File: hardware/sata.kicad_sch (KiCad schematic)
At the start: 26 parts, among them IC1 ASM1061, J9 SATA_22pin, Q2 FDS4435BZ, Q3 FDS4435BZ, Y1 Crystal

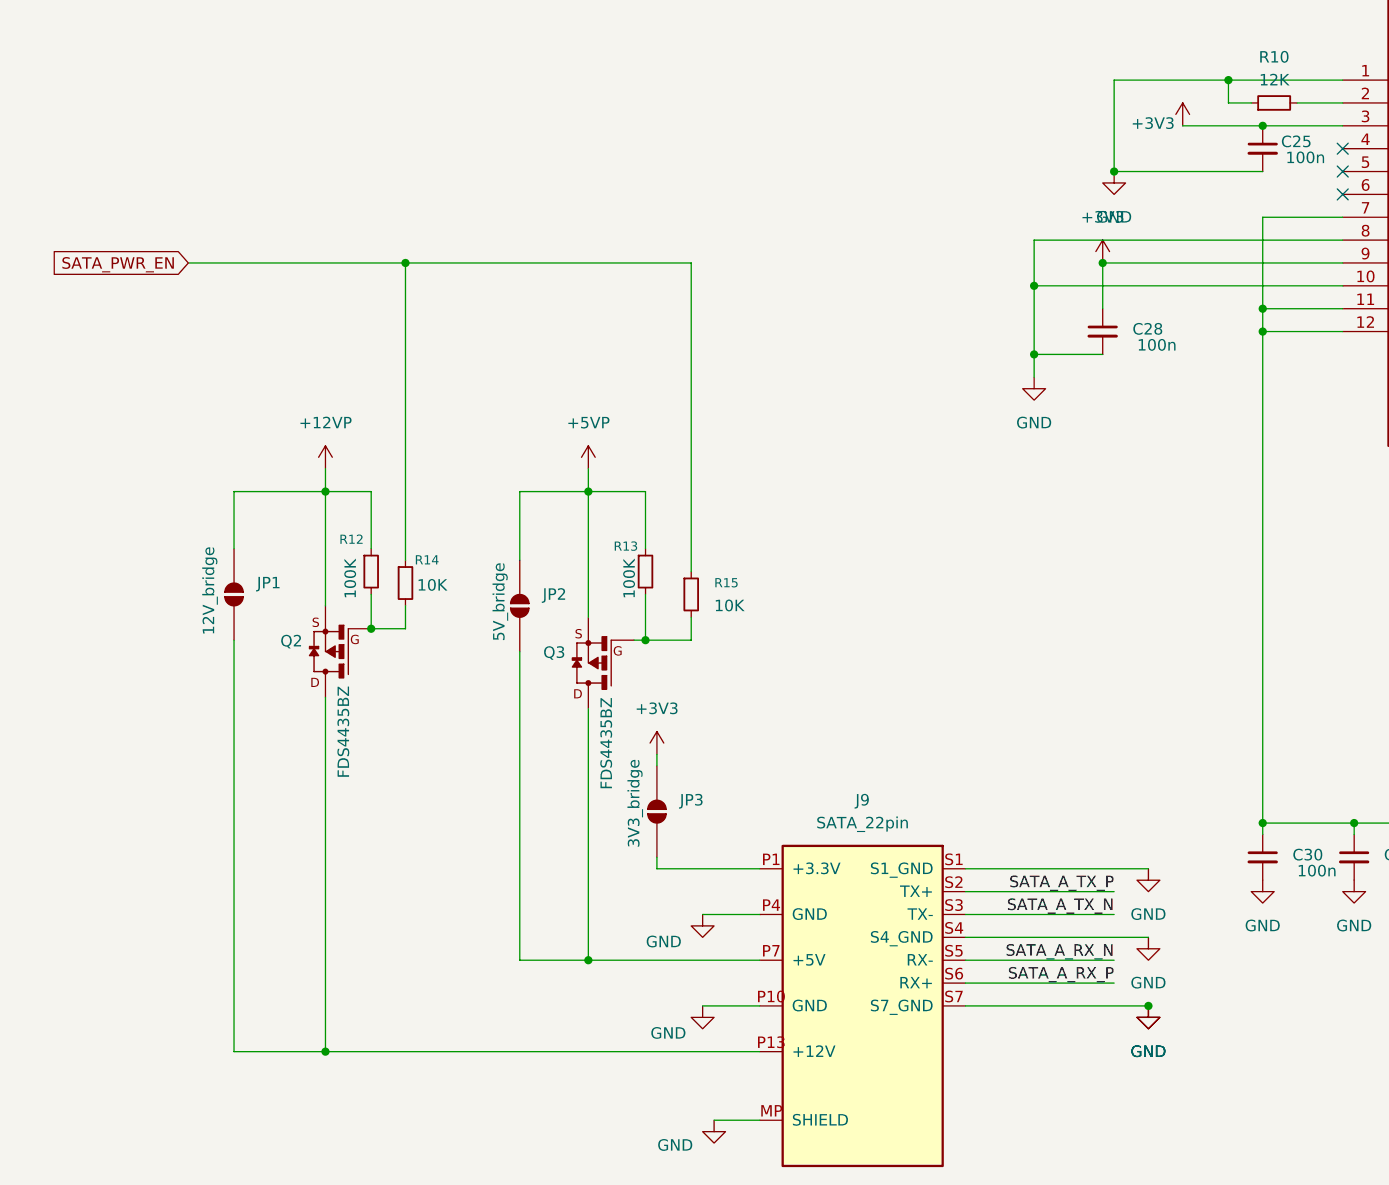
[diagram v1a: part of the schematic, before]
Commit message: SATA power: add N-FET level shifters, solder jumpers, split power netclasses
- Add Q5, Q6 (2N7002) as level shifters between GPIO17 and P-FET gates
  (Q2/Q3). GPIO at 3.3V cannot directly switch P-FETs with 12V/5V sources.
- Add JP5 (SATA_12V_PWR), JP6 (SATA_5V_PWR) 3-pad solder jumpers to
  select boot default: pads 1-2 bridged = HDD off (default), pads 2-3
  bridged = HDD on at boot.
- Add R14 (10K) series gate resistor for GPIO protection against N-FET
  failure.
- Remove old R14, R15 (10K direct GPIO-to-gate resistors) — replaced by
  N-FET level shifter circuit.
- Split Power netclass into Power 12V (3.0mm), Power 5V (2.5mm),
  Power 3V3 (1.0mm) sized for 1oz copper with headroom.
- Update README: document SATA power switching circuit, HDD lifecycle
  scripts, power routing netclasses and guidelines.
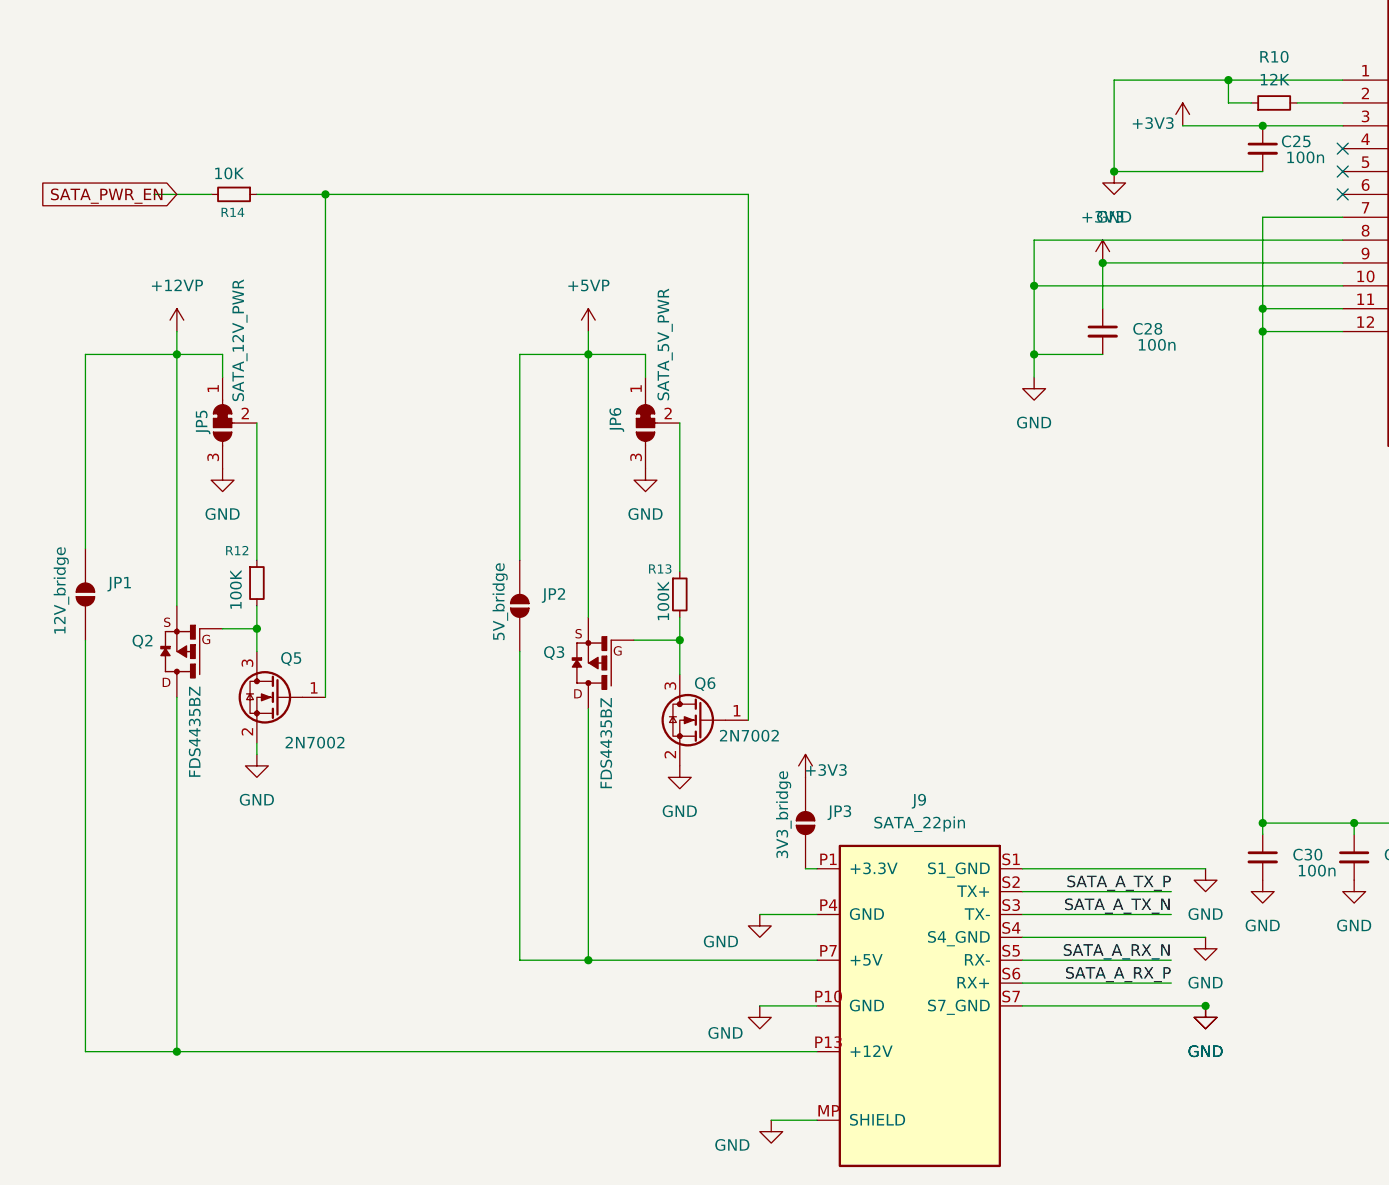
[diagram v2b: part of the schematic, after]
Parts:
- removed R15: 10K, Resistor_SMD:R_0805_2012Metric, symbol Device:R_Small
- added JP5: SATA_12V_PWR, Jumper:SolderJumper-3_P1.3mm_Bridged12_Pad1.0x1.5mm, symbol Jumper:SolderJumper_3_Bridged12
- added JP6: SATA_5V_PWR, Jumper:SolderJumper-3_P1.3mm_Bridged12_Pad1.0x1.5mm, symbol Jumper:SolderJumper_3_Bridged12
- added Q5, Q6: 2N7002, Package_TO_SOT_SMD:SOT-23, symbol Transistor_FET:2N7002
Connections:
- net +12VP: now also JP5.1 (A); no longer R12.1
- net +5VP: now also JP6.1 (A); no longer R13.1
- net GND: now also JP5.3 (B), JP6.3 (B), Q5.2 (S), Q6.2 (S)
- net SATA_PWR_EN: now also R14.2; no longer R14.1
- net at Q3.4, R13.2: now also Q6.3 (D)
- net at Q2.4, R12.2: now also Q5.3 (D); no longer R14.2
- new net: JP6.2 (C), R13.1
- new net: Q5.1 (G), Q6.1 (G), R14.1
- new net: JP5.2 (C), R12.1
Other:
- moved on the sheet: J9, JP1, JP3, Q2, R12, R13

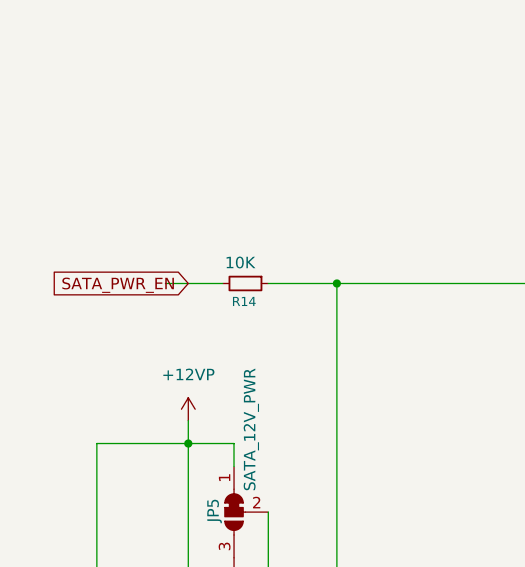
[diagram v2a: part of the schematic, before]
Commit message: Fix mechanical assembly: Part.read() for correct placement, fix PCB/HDD rotations and Z layout
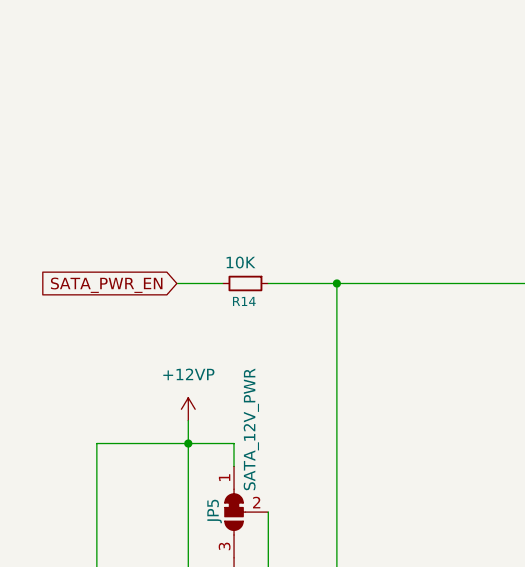
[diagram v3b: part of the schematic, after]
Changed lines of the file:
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@@
-	(wire
-		(pts
-			(xy 27.94 77.47) (xy 34.29 77.47)
-		)
-		(stroke
-			(width 0)
-			(type default)
-		)
-	)
 	(wire
 		(pts
@@
 		(pts
 			(xy 180.34 110.49) (xy 180.34 115.57)
+		)
+		(stroke
+			(width 0)
+			(type default)
+		)
+	)
+	(wire
+		(pts
+			(xy 29.21 77.47) (xy 34.29 77.47)
 		)
 		(stroke
@@
 	(global_label "SATA_PWR_EN"
 		(shape input)
-		(at 30.48 77.47 180)
+		(at 29.21 77.47 180)
 		(fields_autoplaced yes)
 		(effects
@@
 		)
 		(property "Intersheetrefs" "${INTERSHEET_REFS}"
-			(at 14.7344 77.47 0)
+			(at 13.4644 77.47 0)
 			(hide yes)
 			(show_name no)

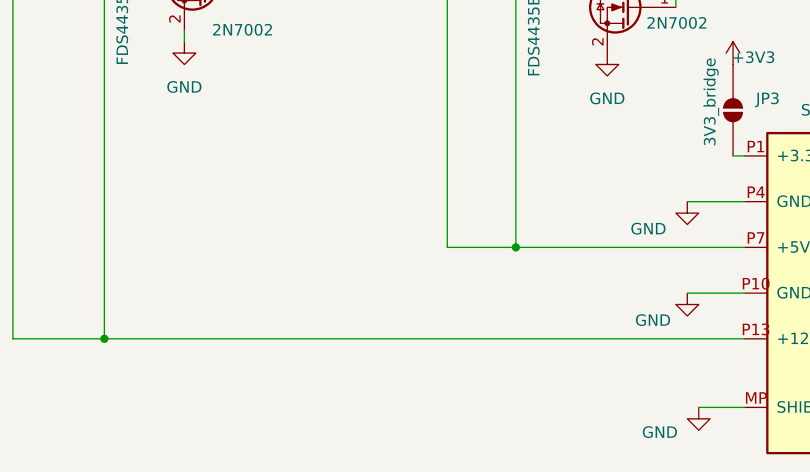
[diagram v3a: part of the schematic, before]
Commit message: Route power distribution and signal nets
5V and 3.3V distribution to CM4, ASM1061, and peripherals.
Additional signal routing for remaining nets.
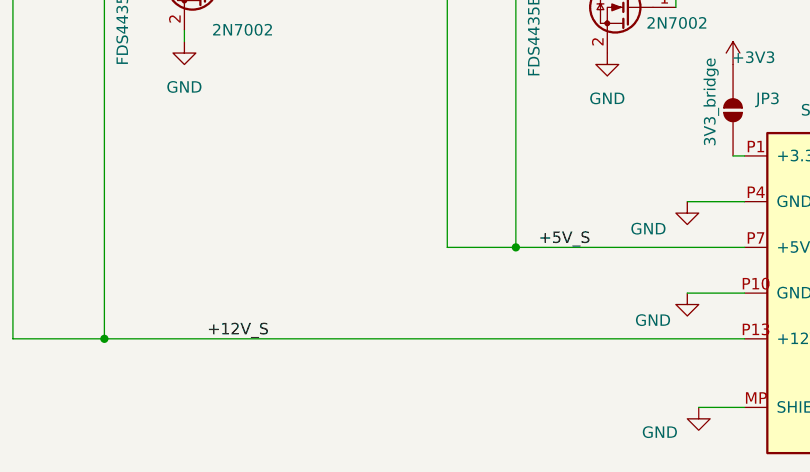
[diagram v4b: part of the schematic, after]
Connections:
- net +12V_S: now reaches J9.P13 (+12V), J9.P14 (+12V), J9.P15 (+12V), JP1.1 (A), Q2.5-8
- net +5V_S: now reaches J9.P7 (+5V), J9.P8 (+5V), J9.P9 (+5V), JP2.1 (A), Q3.5-8
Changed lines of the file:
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@@
+		)
+	)
+	(label "+12V_S"
+		(at 41.91 172.72 0)
+		(effects
+			(font
+				(size 1.27 1.27)
+			)
+			(justify left bottom)
 		)
 	)
@@
 		(effects
 			(font
+				(size 1.27 1.27)
+			)
+			(justify left bottom)
+		)
+	)
+	(label "+5V_S"
+		(at 78.74 162.56 0)
+		(effects
+			(font

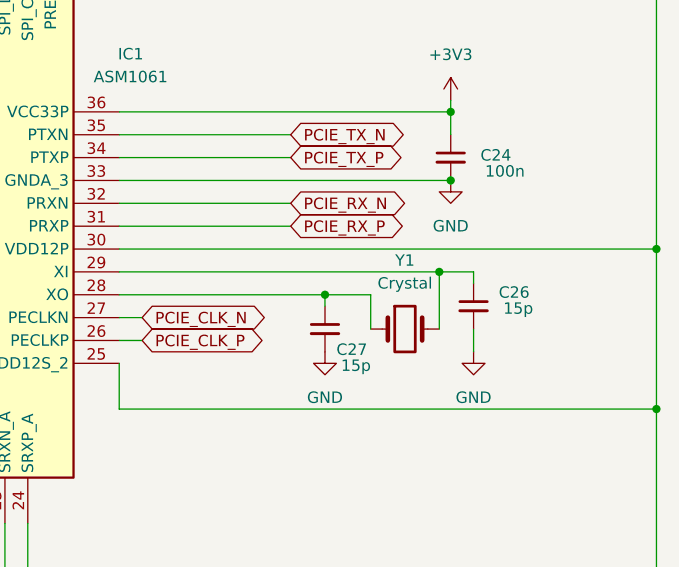
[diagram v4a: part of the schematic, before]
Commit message: fix: add missing BOM values for F1 (3A), Y1 (25MHz), BT1 (CR2032)
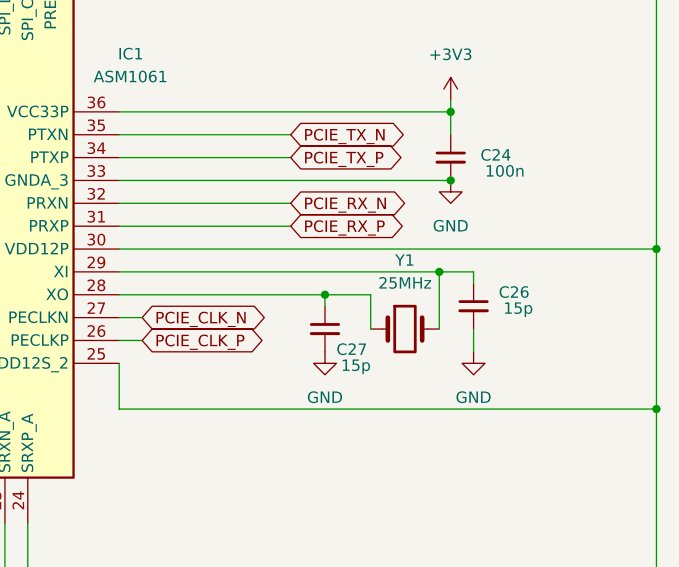
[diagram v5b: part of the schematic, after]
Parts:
- Y1: value Crystal -> 25MHz
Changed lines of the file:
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@@
 			)
 		)
-		(property "Value" "Crystal"
+		(property "Value" "25MHz"
 			(at 237.49 83.82 0)
 			(show_name no)

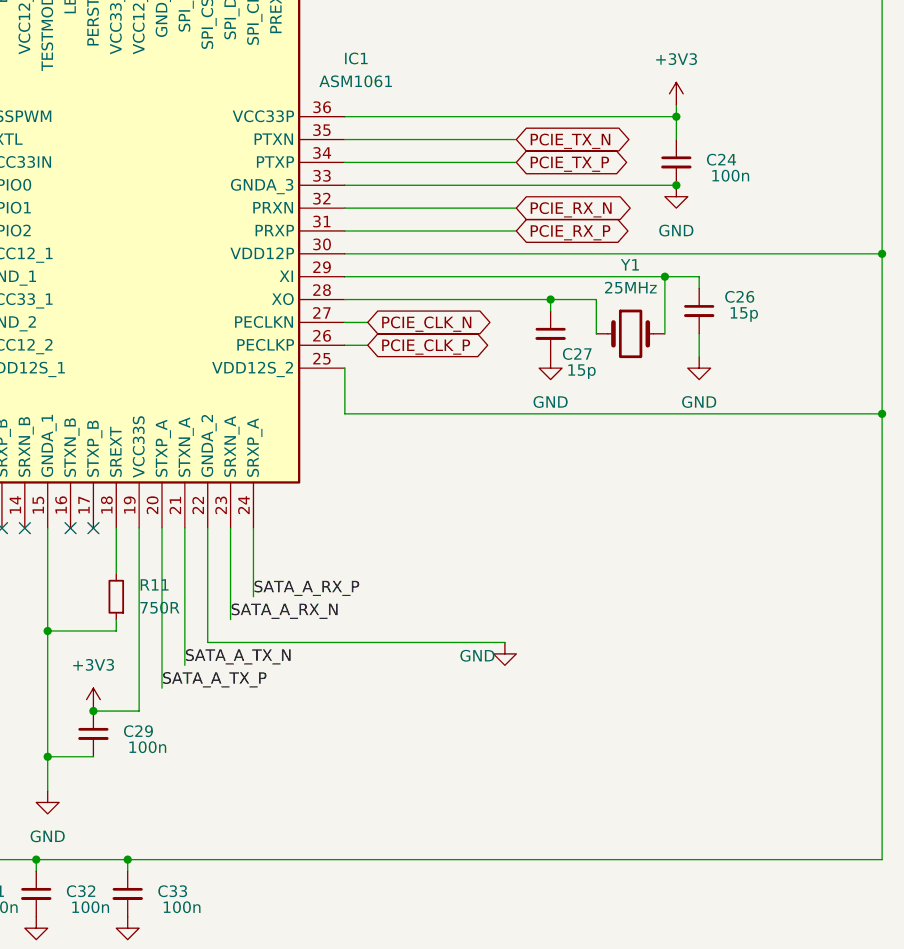
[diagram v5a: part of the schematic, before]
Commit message: feat: add 6 AC coupling caps (C41-C46, 100nF 0805)
- C41-C44: SATA TX/RX pairs (STXP_A, STXN_A, SRXP_A, SRXN_A)
- C45-C46: PCIe RX pair (PCIE_RX_P, PCIE_RX_N)
All placed near ASM1061 per datasheet requirements.
ERC: 0 errors, 0 warnings.
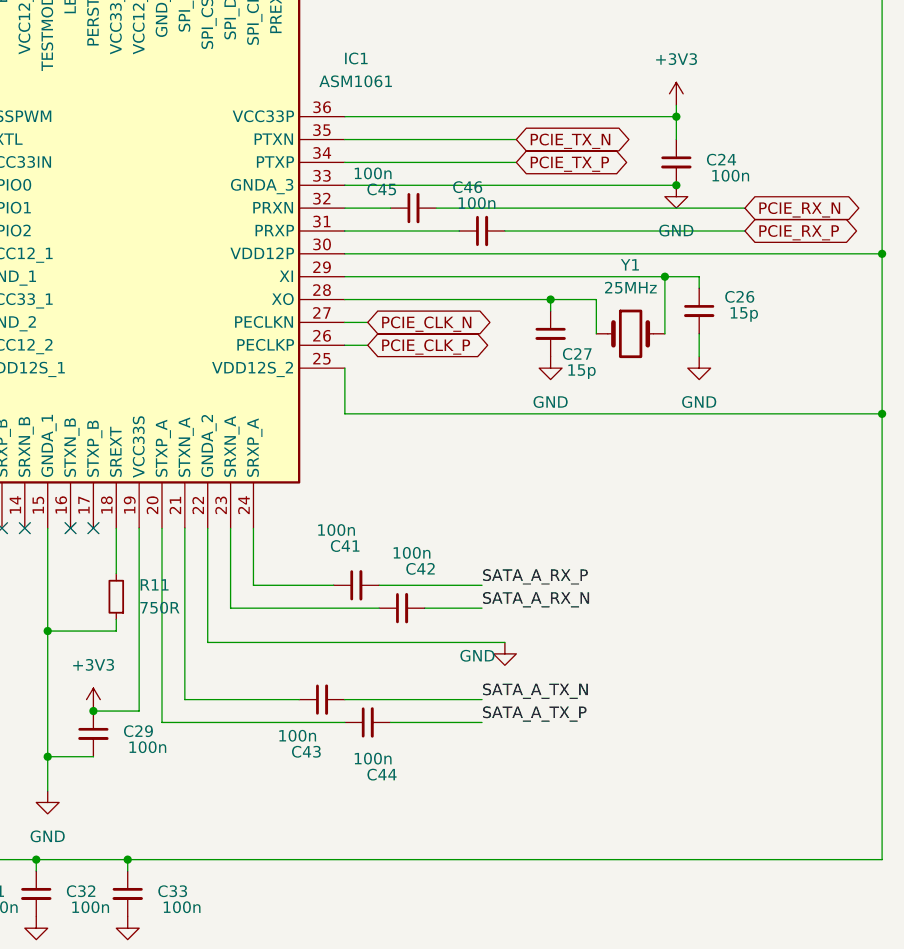
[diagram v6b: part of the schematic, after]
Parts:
- added C41, C42, C43, C44, C45, C46: 100n, Capacitor_SMD:C_0805_2012Metric, symbol Device:C_Small
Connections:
- net PCIE_RX_N: now also C45.2; no longer IC1.32 (PRXN)
- net PCIE_RX_P: now also C46.2; no longer IC1.31 (PRXP)
- net SATA_A_RX_N: now also C42.2; no longer IC1.23 (SRXN_A)
- net SATA_A_RX_P: now also C41.2; no longer IC1.24 (SRXP_A)
- net SATA_A_TX_N: now also C43.2; no longer IC1.21 (STXN_A)
- net SATA_A_TX_P: now also C44.2; no longer IC1.20 (STXP_A)
- new net: C42.1, IC1.23 (SRXN_A)
- new net: C45.1, IC1.32 (PRXN)
- new net: C41.1, IC1.24 (SRXP_A)
- new net: C43.1, IC1.21 (STXN_A)
- new net: C46.1, IC1.31 (PRXP)
- new net: C44.1, IC1.20 (STXP_A)
